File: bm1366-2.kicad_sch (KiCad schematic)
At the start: 88 parts, among them U1 25MHz, U13 ADP171AUJ-R7, U18 TLV3544, U19 BM1366_mode0, U22 BM1366_mode0, U23 ADP171AUJ-R7

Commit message: BOM mostly completed
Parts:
- R6: DK (none) -> 13-RC0402FR-136K8LCT-ND; PARTNO (none) -> RC0402FR-136K8L
- R6: DK (none) -> 311-33.0LRCT-ND; PARTNO (none) -> RC0402FR-0733RL
- R6: value 10K -> 10k; DK (none) -> 311-10KJRCT-ND; PARTNO (none) -> RC0402JR-0710KL
- R6: value 182K -> 182k 1%; DK (none) -> YAG3015CT-ND; PARTNO (none) -> RC0402FR-07182KL; Tolerance 1% -> (none)
- R6: value 130K -> 130k 1%; DK (none) -> YAG2969CT-ND; PARTNO (none) -> RC0402FR-07130KL; Tolerance 1% -> (none)
- R6: DK (none) -> 311-0.0JRCT-ND; PARTNO (none) -> RC0402JR-070RL
- R6: value 1K -> 1k; DK (none) -> 311-1.00KLRCT-ND; PARTNO (none) -> RC0402FR-071KL
- R6: value 309K -> 309k 1%; DK (none) -> YAG3108CT-ND; PARTNO (none) -> RC0402FR-07309KL; Tolerance 1% -> (none)
- R62, R68: DK (none) -> 311-1.00LRCT-ND; PARTNO (none) -> RC0402FR-071RL
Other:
- title: bitaxeUltraHex -> bitaxeHex

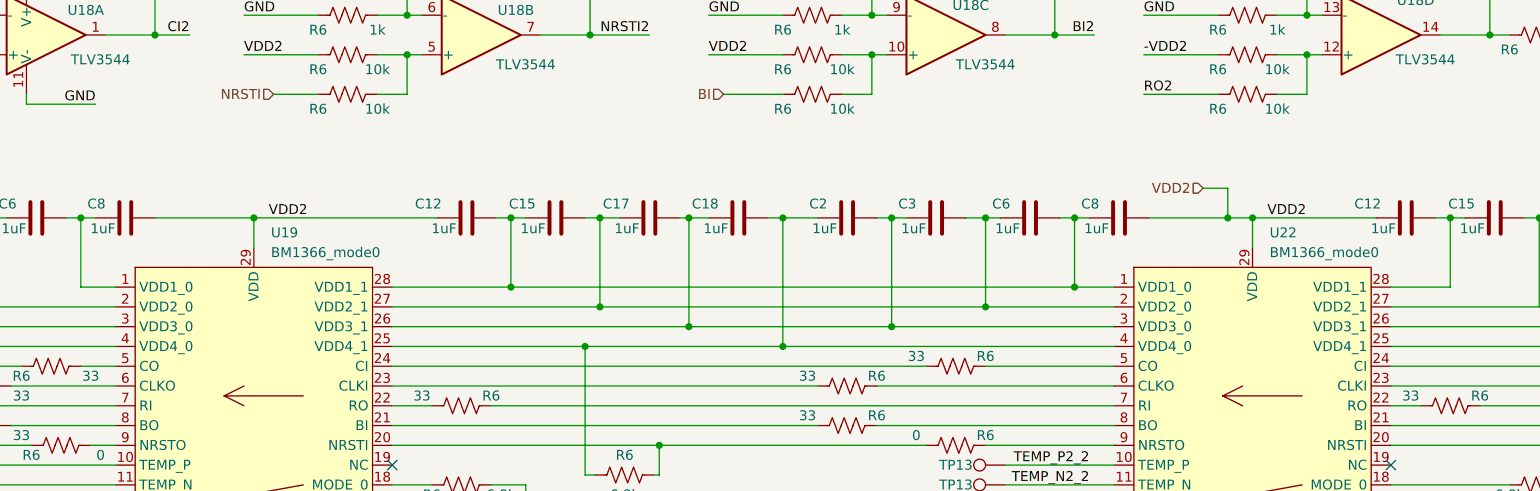
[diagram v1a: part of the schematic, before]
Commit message: link heatsink to schematic and re-link heatsink mounting holes :P
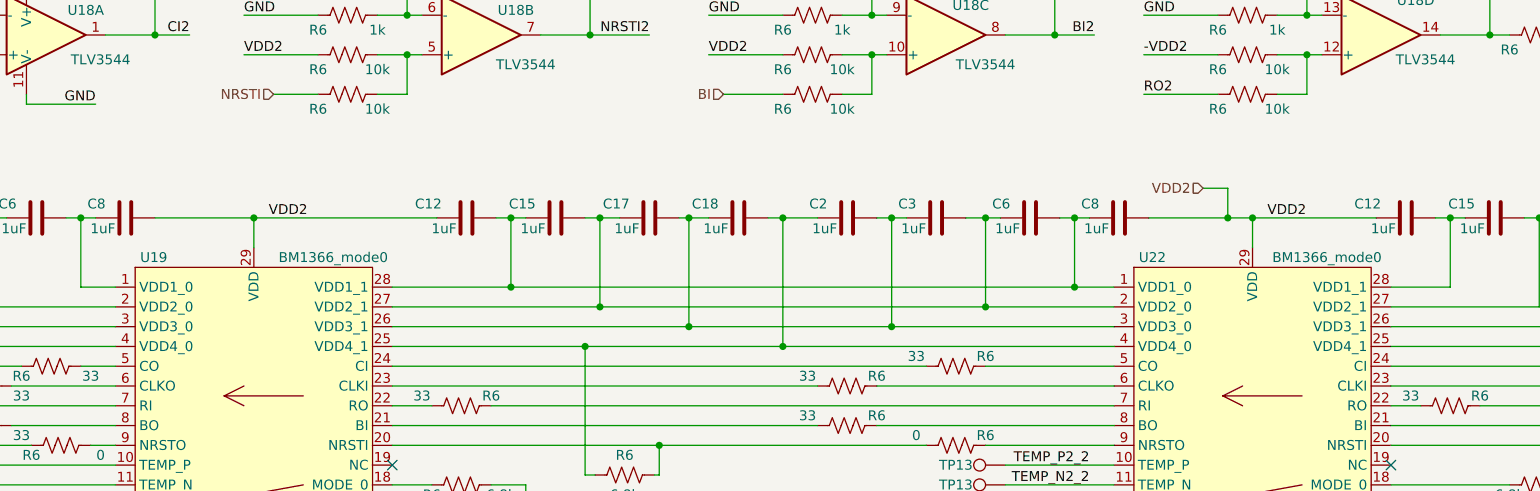
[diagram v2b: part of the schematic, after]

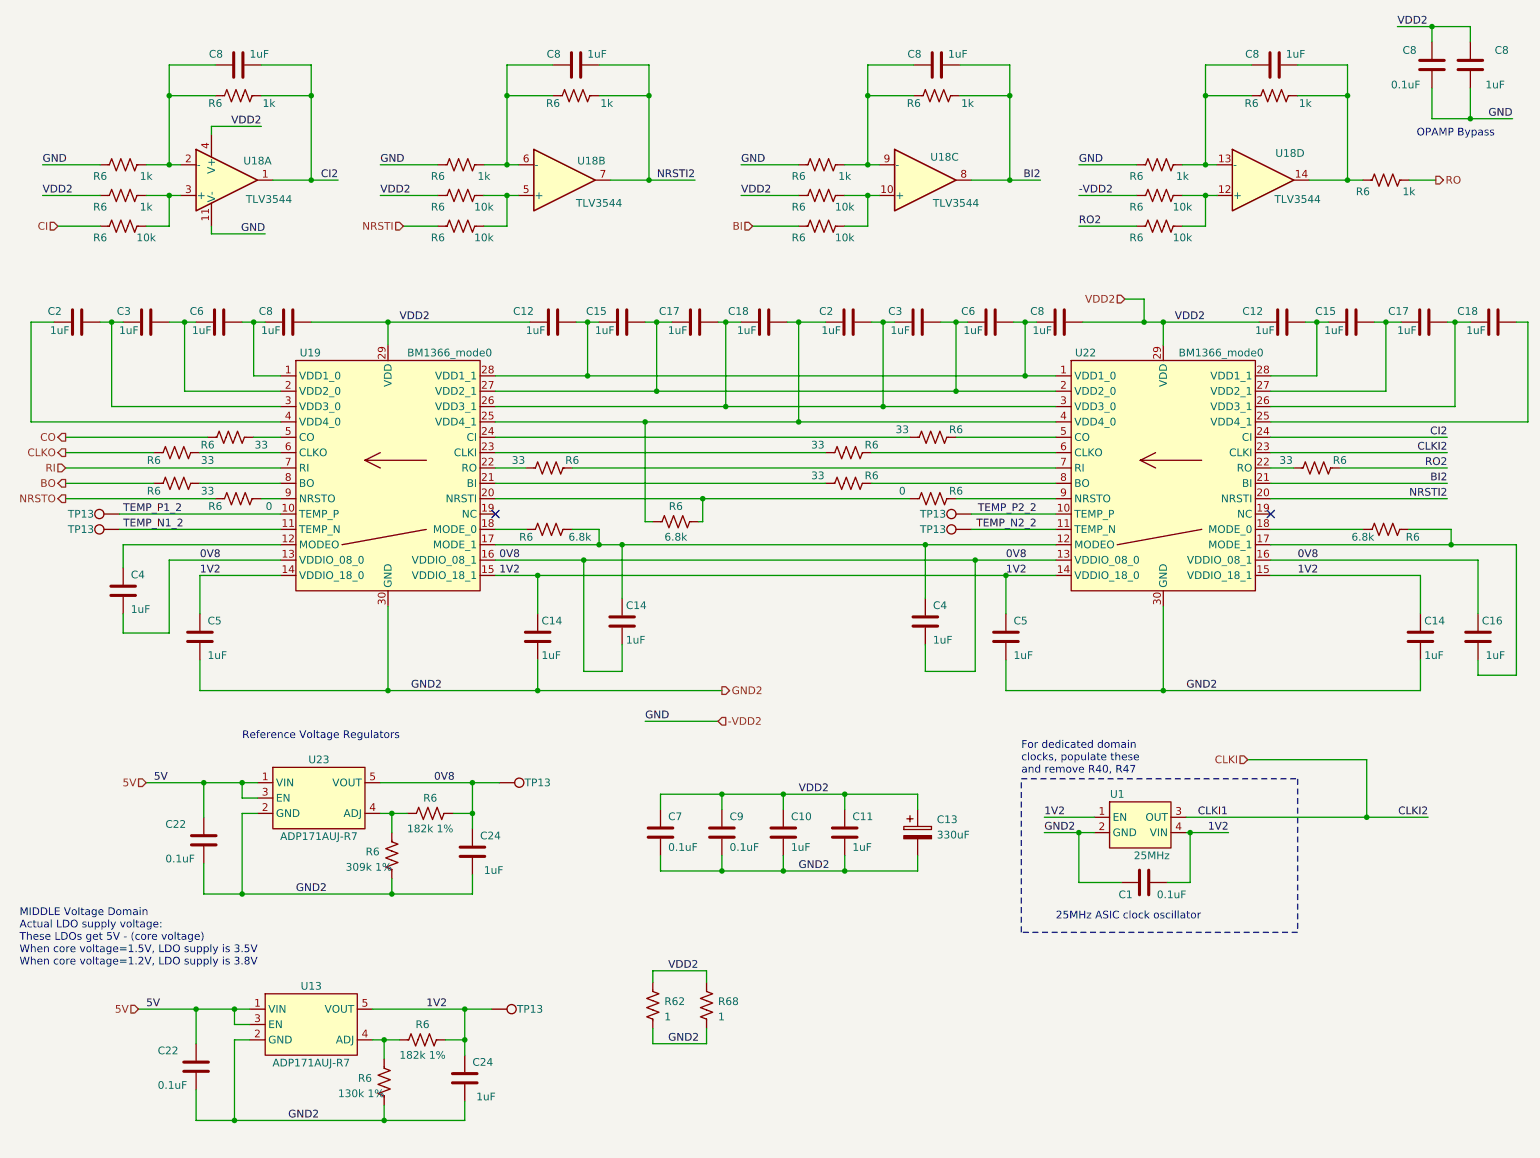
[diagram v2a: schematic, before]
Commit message: sorting out new info on the BM1366 pinouts
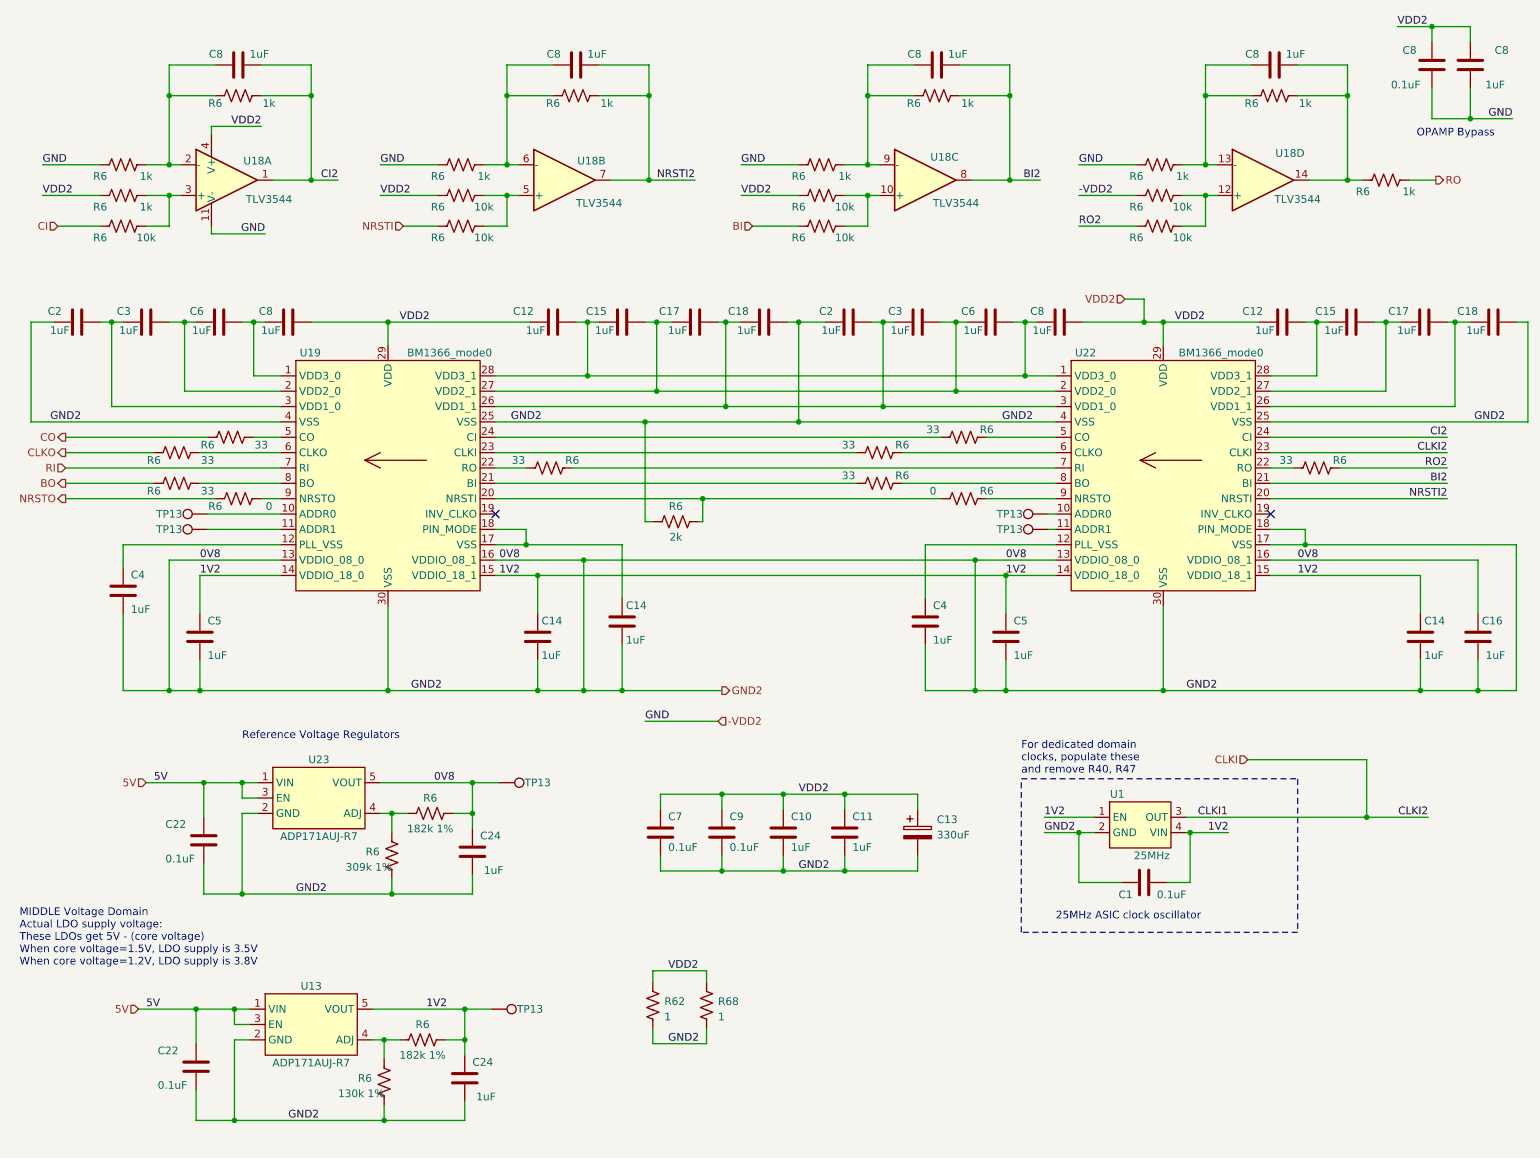
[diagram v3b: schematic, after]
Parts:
- removed R6 (x2): 6.8k, Resistor_SMD:R_0402_1005Metric, symbol Device:R_US
- R6: value 6.8k -> 2k; DK 13-RC0402FR-136K8LCT-ND -> (none); PARTNO RC0402FR-136K8L -> (none)
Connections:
- net 0V8 is gone; now on net GND2: C14.2, C16.1, C24.1, C4.2, C4.2, R6.1, TP13.1, U19.13 (VDDIO_08_0), U19.16 (VDDIO_08_1), U22.13 (VDDIO_08_0), U22.16 (VDDIO_08_1), U23.5 (VOUT)
- net GND2: now also C16.2, C18.2, C18.2, C2.1, C2.1, R6.1, U19.25 (VSS), U19.4 (VSS), U22.17 (VSS), U22.18 (PIN_MODE), U22.25 (VSS), U22.4 (VSS)
- net at C14.1, U19.17 (VSS): now also U19.18 (PIN_MODE); no longer C4.1, U22.12 (MODEO)
- net TEMP_N1_2: no longer names the net of TP13.1, U19.11 (ADDR1)
- net TEMP_N2_2: no longer names the net of TP13.1, U22.11 (ADDR1)
- net TEMP_P1_2: no longer names the net of TP13.1, U19.10 (ADDR0)
- net TEMP_P2_2: no longer names the net of TP13.1, U22.10 (ADDR0)
- new net: C4.1, U22.12 (PLL_VSS)
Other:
- moved on the sheet: R6, TP13

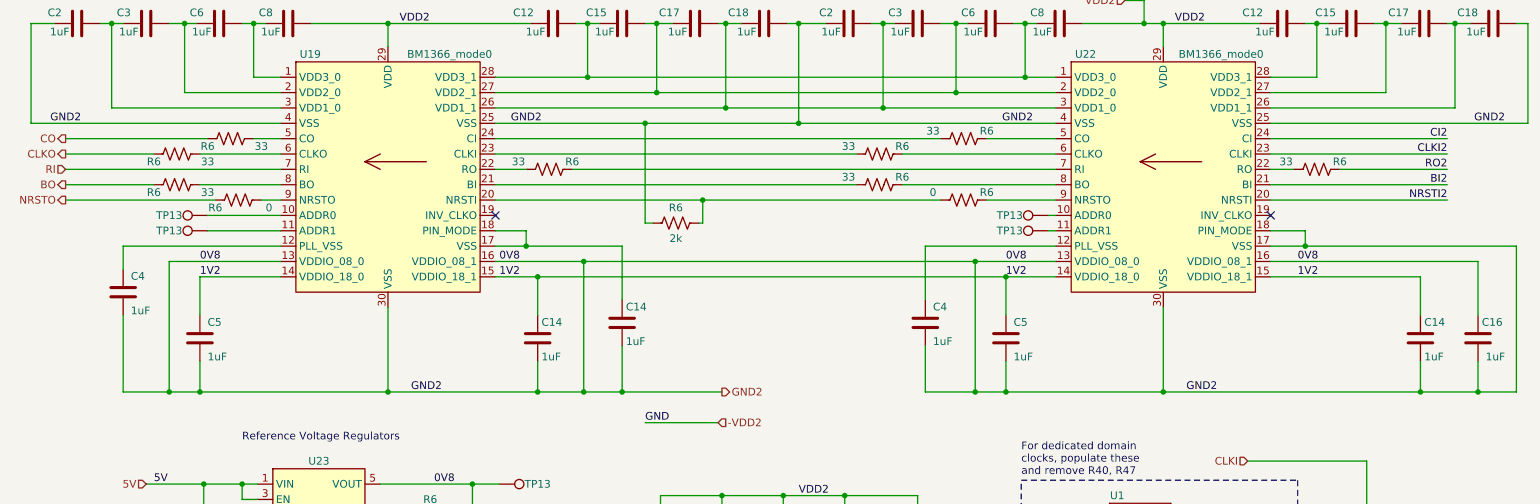
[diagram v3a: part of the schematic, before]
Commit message: routed 1366 changes
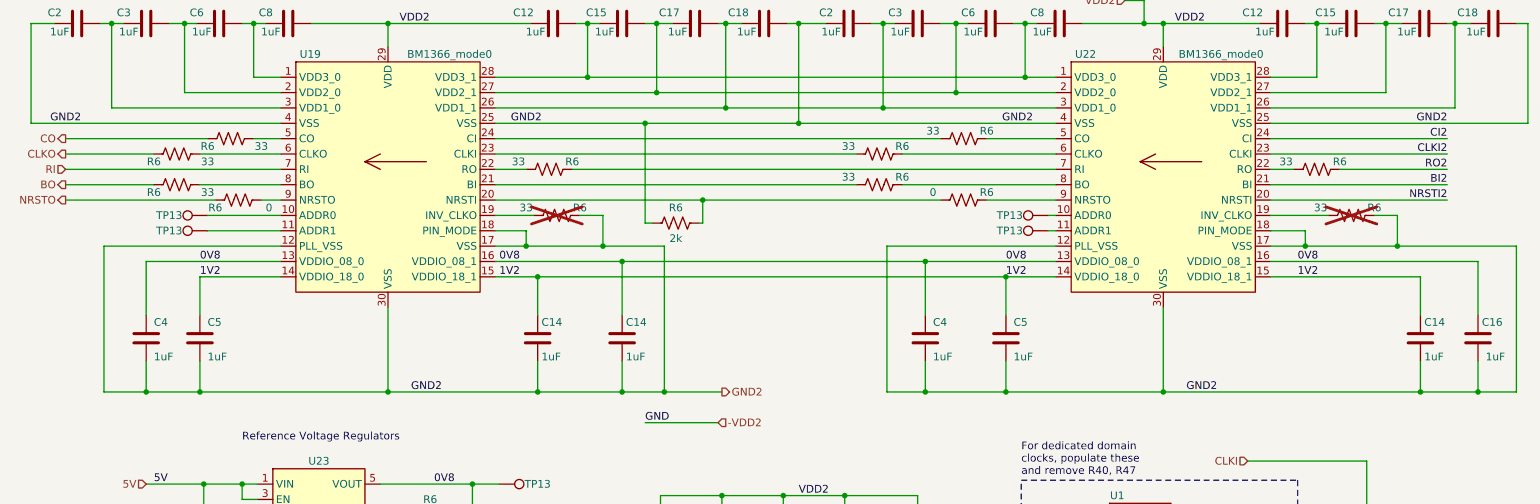
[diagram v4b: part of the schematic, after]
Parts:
- added R6 (x2): 33, Resistor_SMD:R_0402_1005Metric, symbol Device:R_US
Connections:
- net GND2: now also U19.12 (PLL_VSS), U19.17 (VSS), U19.18 (PIN_MODE), U22.12 (PLL_VSS), R6.2, R6.2; no longer C16.1, C24.1, R6.1, TP13.1, U19.13 (VDDIO_08_0), U19.16 (VDDIO_08_1), U22.13 (VDDIO_08_0), U22.16 (VDDIO_08_1), U23.5 (VOUT)
- net 0V8: now reaches C4.1
- net 0V8: now also C14.1, C16.1, C24.1, C4.1, R6.1, TP13.1, U19.13 (VDDIO_08_0), U19.16 (VDDIO_08_1), U22.13 (VDDIO_08_0), U22.16 (VDDIO_08_1), U23.5 (VOUT); no longer U19.12 (PLL_VSS)
- net at U19.19 (INV_CLKO): now also R6.1
- net at U22.19 (INV_CLKO): now also R6.1
- no-connect marks 2 -> 0
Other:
- moved on the sheet: C14, C4

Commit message: Fix some part numbers in the BOM
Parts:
- R6: DK (none) -> YAG2303CT-ND; PARTNO (none) -> RT0402BRD072KL
- R62, R68: DK 311-1.00LRCT-ND -> 118-CR2512-F/-1R00ELFCT-ND; PARTNO RC0402FR-071RL -> CR2512-F/-1R00ELF
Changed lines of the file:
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@@
       (effects (font (size 1.27 1.27)) hide)
     )
-    (property "DK" "" (at 125.095 99.695 0)
+    (property "DK" "YAG2303CT-ND" (at 125.095 99.695 0)
       (effects (font (size 1.27 1.27)) hide)
     )
-    (property "PARTNO" "" (at 125.095 99.695 0)
+    (property "PARTNO" "RT0402BRD072KL" (at 125.095 99.695 0)
       (effects (font (size 1.27 1.27)) hide)
     )
@@
       (effects (font (size 1.27 1.27)) hide)
     )
-    (property "DK" "311-1.00LRCT-ND" (at 121.285 179.705 0)
+    (property "DK" "118-CR2512-F/-1R00ELFCT-ND" (at 121.285 179.705 0)
       (effects (font (size 1.27 1.27)) hide)
     )
-    (property "PARTNO" "RC0402FR-071RL" (at 121.285 179.705 0)
+    (property "PARTNO" "CR2512-F/-1R00ELF" (at 121.285 179.705 0)
       (effects (font (size 1.27 1.27)) hide)
     )
@@
       (effects (font (size 1.27 1.27)) hide)
     )
-    (property "DK" "311-1.00LRCT-ND" (at 130.175 179.705 0)
+    (property "DK" "118-CR2512-F/-1R00ELFCT-ND" (at 130.175 179.705 0)
       (effects (font (size 1.27 1.27)) hide)
     )
-    (property "PARTNO" "RC0402FR-071RL" (at 130.175 179.705 0)
+    (property "PARTNO" "CR2512-F/-1R00ELF" (at 130.175 179.705 0)
       (effects (font (size 1.27 1.27)) hide)
     )

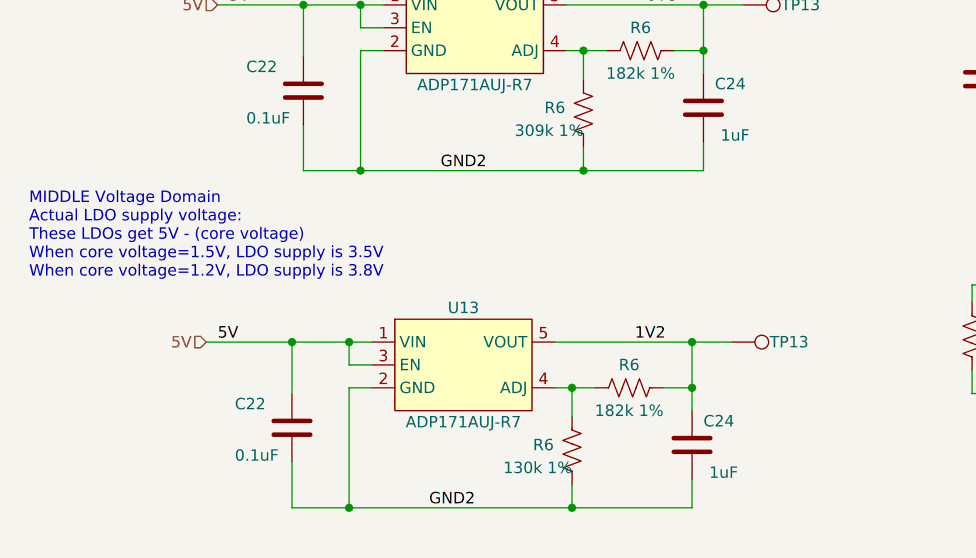
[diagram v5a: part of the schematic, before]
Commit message: add option for 1.5V ASIC Vref
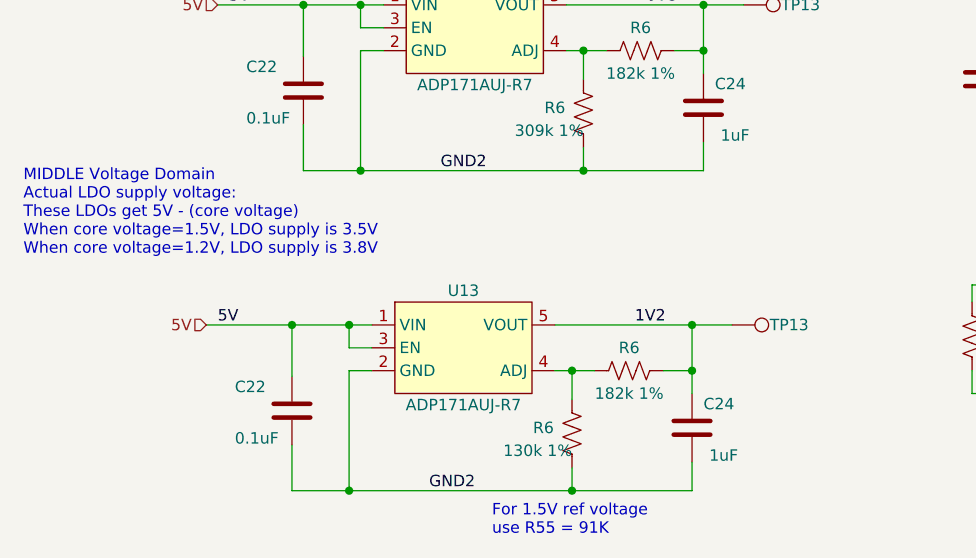
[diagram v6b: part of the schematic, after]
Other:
- note added: "For 1.5V ref voltage use R55 = 91K"
- moved on the sheet: C22, C24, R6, TP13, U13

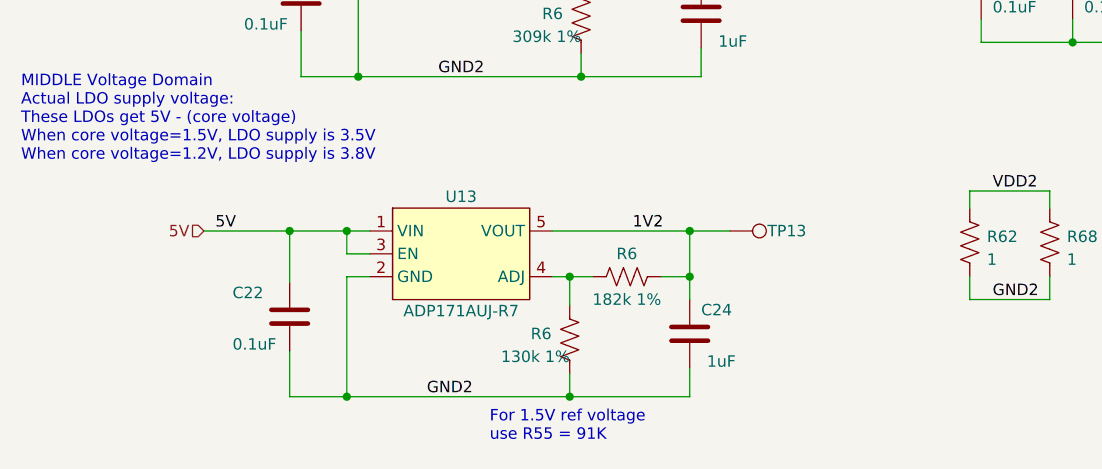
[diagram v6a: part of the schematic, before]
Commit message: add note to specify resistor value for 1.8V reference voltage
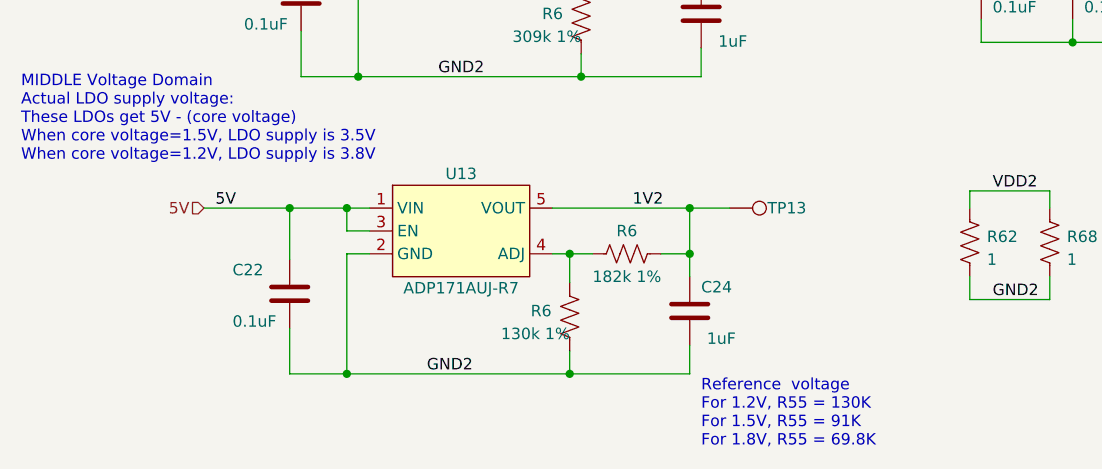
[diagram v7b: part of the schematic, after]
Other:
- note added: "Reference voltage For 1.2V, R55 = 130K For 1.5V, R55 = 91K For 1.8V, R55 = 69.8K"
- note removed: "For 1.5V ref voltage use R55 = 91K"
- moved on the sheet: C22, C24, R6, TP13, U13
